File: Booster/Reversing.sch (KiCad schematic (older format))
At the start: 22 parts

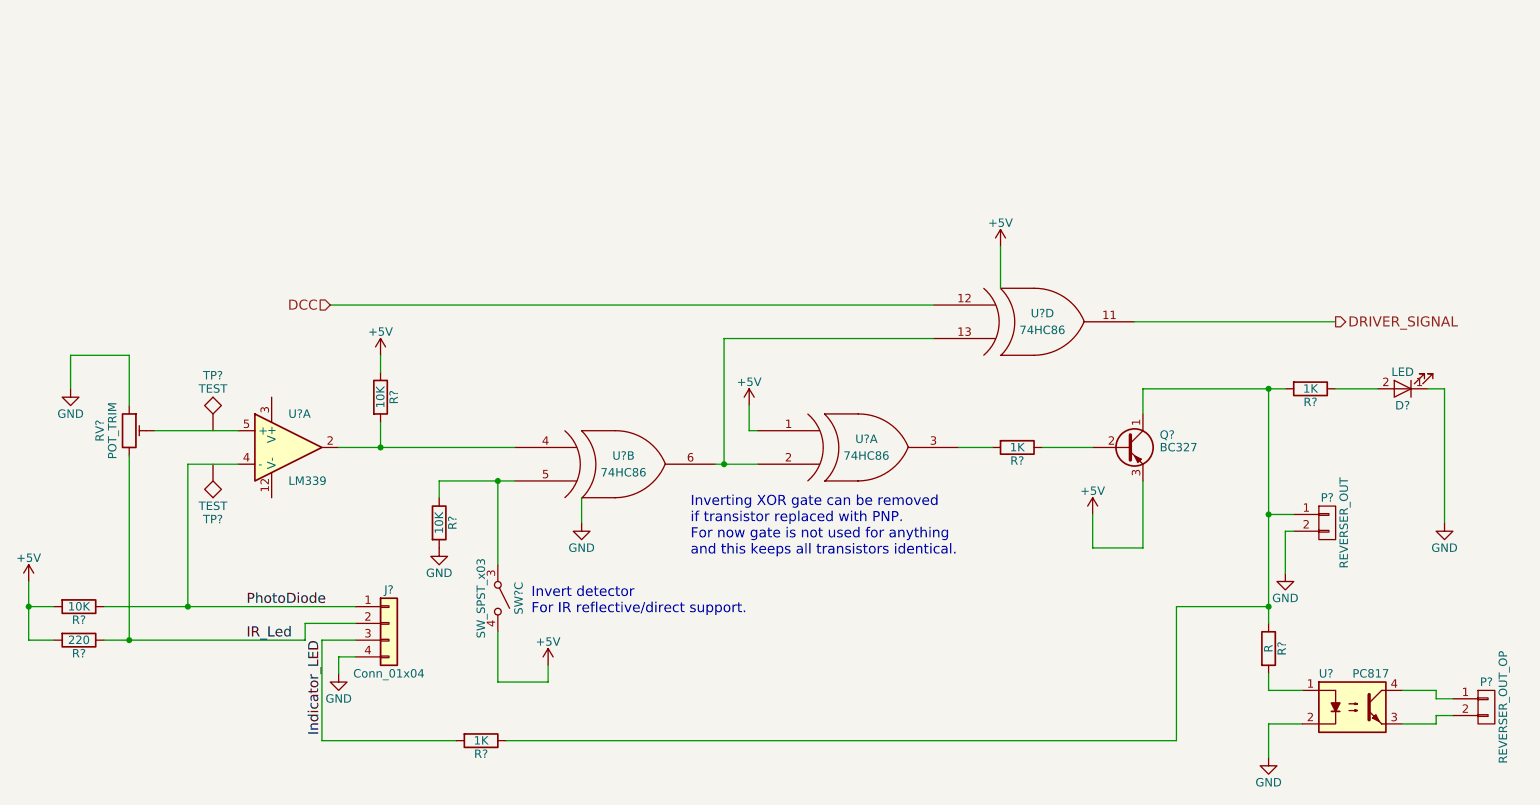
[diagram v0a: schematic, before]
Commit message: Fixed missing connections.
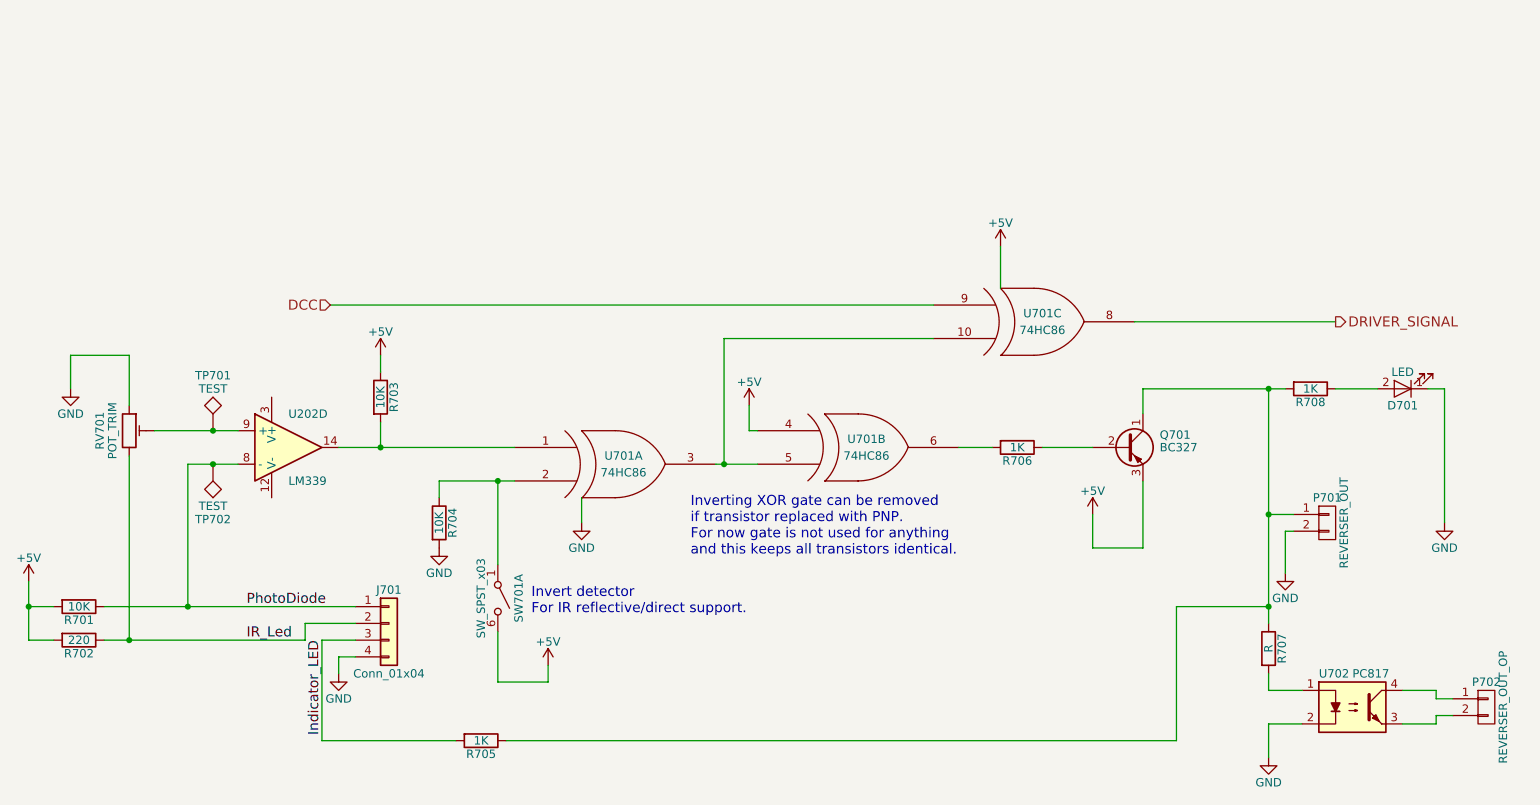
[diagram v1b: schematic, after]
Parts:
- gave numbers to parts that had none: 20
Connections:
- net +5V: now also SW701.6 (B), U701.4 (IN1); no longer SW701.4 (B), U701.1 (IN1)
- net DCC: now also U701.9 (IN1); no longer U701.12 (IN1)
- net DRIVER_SIGNAL: now also U701.8 (OUT); no longer U701.11 (OUT)
- net PhotoDiode: now also TP702.1, U202.8 (-); no longer U202.4 (-)
- net at RV701.2: now also TP701.1, U202.9 (+); no longer U202.5 (+)
- net at R706.2: now also U701.6 (OUT); no longer U701.3 (OUT)
- new net: U701.10 (IN2), U701.3 (OUT), U701.5 (IN2)
- new net: R703.2, U202.14, U701.1 (IN1)
- new net: R704.1, SW701.1 (A), U701.2 (IN2)

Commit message: Pulse detector circuit included.
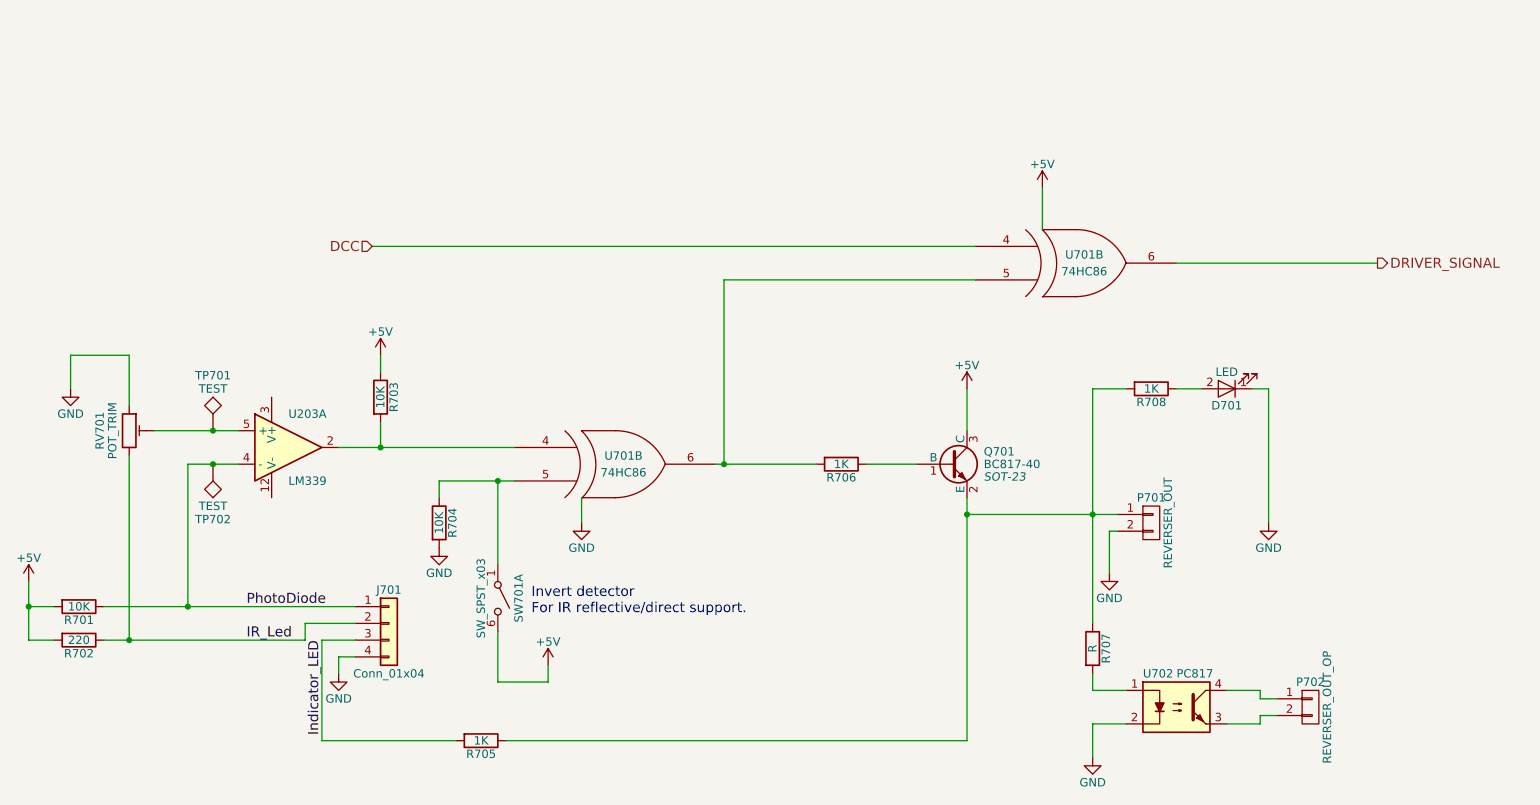
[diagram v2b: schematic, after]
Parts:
- removed Q701: BC327, TO_SOT_Packages_THT:TO-92_Molded_Narrow, symbol BC327
- removed unit 2 of U701
- added Q701: BC817-40, SOT-23, symbol BC817-40
- renumbered U202 to U203
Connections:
- net +5V: now also Q701.3 (C)
- net DCC: now also U701.4 (IN1); no longer U701.9 (IN1)
- net DRIVER_SIGNAL: now also U701.6 (OUT); no longer U701.8 (OUT)
- net PhotoDiode: now also U203.4 (-); no longer U203.8 (-)
- net at RV701.2, TP701.1: now also U203.5 (+); no longer U203.9 (+)
- net at R706.1: now also Q701.1 (B)
- net at R706.2: now also U701.5 (IN2), U701.6 (OUT)
- net at P701.1 (P1), R705.1, R707.1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: now also Q701.2 (E)
- net at R704.1, SW701.1 (A): now also U701.5 (IN2); no longer U701.2 (IN2)
- new net: R703.2, U203.2, U701.4 (IN1)
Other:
- note removed: "Inverting XOR gate can be removed\nif transistor replaced with PNP.\nFor now gate is not used for anything\nand this keeps all transistors identical."
- moved on the sheet: D701, P701, P702, R706, R707, R708, U702

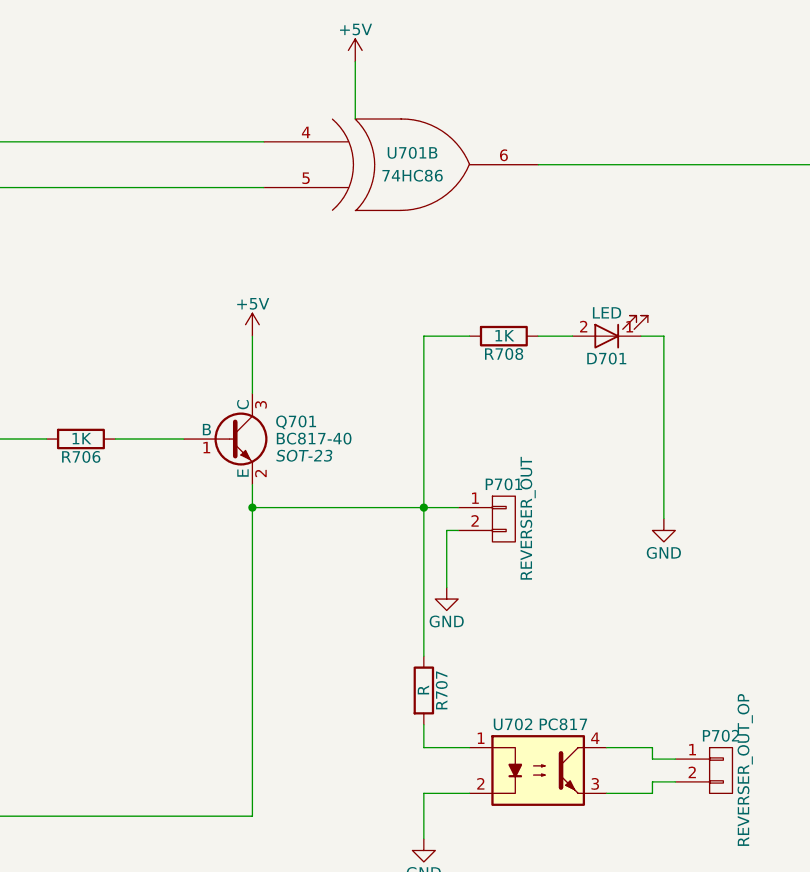
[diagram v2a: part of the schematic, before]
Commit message: Various adjustments based on breadboard prototype.
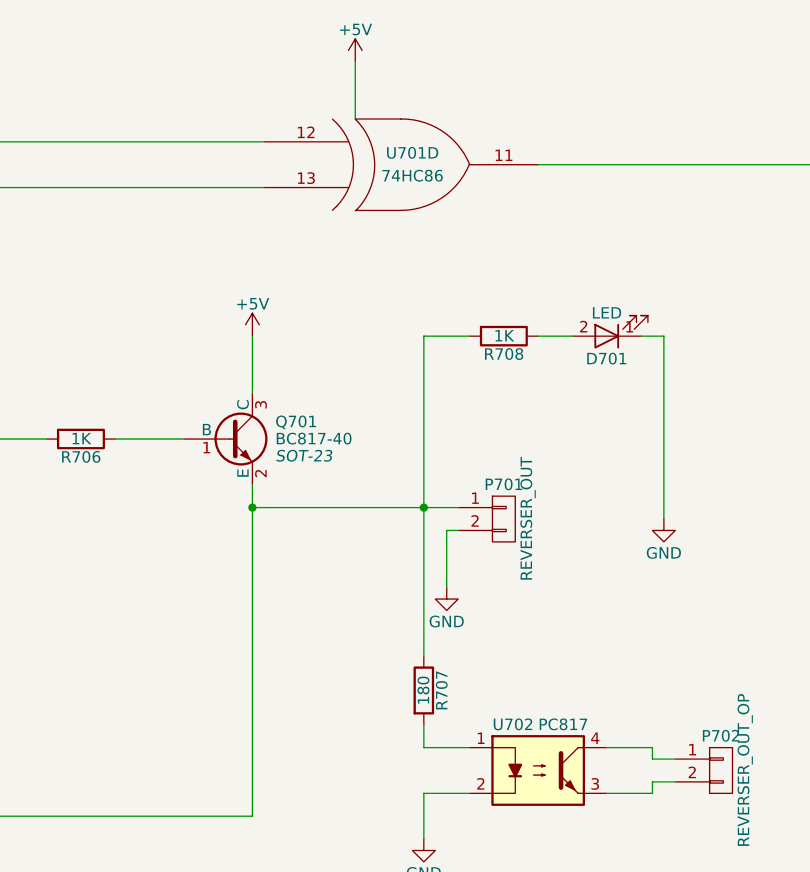
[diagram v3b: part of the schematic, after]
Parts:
- R707: value R -> 180
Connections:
- net DCC: now also U701.12 (IN1); no longer U701.4 (IN1)
- net DRIVER_SIGNAL: now also U701.11 (OUT); no longer U701.6 (OUT)
- net at R706.2, U701.6 (OUT): now also U701.13 (IN2); no longer U701.5 (IN2)
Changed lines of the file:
@@
 $Comp
 L 74LS86 U701
-U 2 1 5A0898F2
+U 4 1 5A0898F2
 P 8200 2250
 F 0 "U701" H 8250 2300 50  0000 C CNN
@@
 F 2 "" H 8200 2250 50  0000 C CNN
 F 3 "" H 8200 2250 50  0000 C CNN
-	2    8200 2250
+	4    8200 2250
 	1    0    0    -1
 $EndComp
@@
 $EndComp
 $Comp
-L +5V #PWR704
+L +5V #PWR053
 U 1 1 5A08A3B3
 P 4050 2800
-F 0 "#PWR704" H 4050 2650 50  0001 C CNN
+F 0 "#PWR053" H 4050 2650 50  0001 C CNN
 F 1 "+5V" H 4050 2940 50  0000 C CNN
 F 2 "" H 4050 2800 50  0000 C CNN
@@
 $EndComp
 $Comp
-L +5V #PWR708
+L +5V #PWR054
 U 1 1 5A08AC26
 P 7550 3000
-F 0 "#PWR708" H 7550 2850 50  0001 C CNN
+F 0 "#PWR054" H 7550 2850 50  0001 C CNN
 F 1 "+5V" H 7550 3140 50  0000 C CNN
 F 2 "" H 7550 3000 50  0000 C CNN
@@
 $EndComp
 $Comp
-L GND #PWR712
+L GND #PWR055
 U 1 1 5A08AC50
 P 9350 3800
-F 0 "#PWR712" H 9350 3550 50  0001 C CNN
+F 0 "#PWR055" H 9350 3550 50  0001 C CNN
 F 1 "GND" H 9350 3650 50  0000 C CNN
 F 2 "" H 9350 3800 50  0000 C CNN
@@
 $EndComp
 $Comp
-L GND #PWR711
+L GND #PWR056
 U 1 1 5A0EF583
 P 8400 4100
-F 0 "#PWR711" H 8400 3850 50  0001 C CNN
+F 0 "#PWR056" H 8400 3850 50  0001 C CNN
 F 1 "GND" H 8400 3950 50  0000 C CNN
 F 2 "" H 8400 4100 50  0001 C CNN
@@
 P 8300 4550
 F 0 "R707" V 8380 4550 50  0000 C CNN
-F 1 "R" V 8300 4550 50  0000 C CNN
+F 1 "180" V 8300 4550 50  0000 C CNN
 F 2 "" V 8230 4550 50  0001 C CNN
 F 3 "" H 8300 4550 50  0001 C CNN
@@
 $EndComp
 $Comp
-L GND #PWR710
+L GND #PWR057
 U 1 1 5A0EF7FA
 P 8300 5200
-F 0 "#PWR710" H 8300 4950 50  0001 C CNN
+F 0 "#PWR057" H 8300 4950 50  0001 C CNN
 F 1 "GND" H 8300 5050 50  0000 C CNN
 F 2 "" H 8300 5200 50  0001 C CNN
@@
 $EndComp
 $Comp
-L GND #PWR705
+L GND #PWR058
 U 1 1 5A0F5794
 P 4400 3950
-F 0 "#PWR705" H 4400 3700 50  0001 C CNN
+F 0 "#PWR058" H 4400 3700 50  0001 C CNN
 F 1 "GND" H 4400 3800 50  0000 C CNN
 F 2 "" H 4400 3950 50  0000 C CNN
@@
 $EndComp
 $Comp
-L +5V #PWR706
+L +5V #PWR059
 U 1 1 5A0F5A28
 P 5050 4650
-F 0 "#PWR706" H 5050 4500 50  0001 C CNN
+F 0 "#PWR059" H 5050 4500 50  0001 C CNN
 F 1 "+5V" H 5050 4790 50  0000 C CNN
 F 2 "" H 5050 4650 50  0001 C CNN
@@
 IR_Led
 $Comp
-L +5V #PWR709
+L +5V #PWR060
 U 1 1 5A0FEE2F
 P 8000 1800
-F 0 "#PWR709" H 8000 1650 50  0001 C CNN
+F 0 "#PWR060" H 8000 1650 50  0001 C CNN
 F 1 "+5V" H 8000 1940 50  0000 C CNN
 F 2 "" H 8000 1800 50  0001 C CNN
@@
 	3800 4600 3800 4700
 $Comp
-L GND #PWR703
+L GND #PWR061
 U 1 1 5A101A8A
 P 3800 4700
-F 0 "#PWR703" H 3800 4450 50  0001 C CNN
+F 0 "#PWR061" H 3800 4450 50  0001 C CNN
 F 1 "GND" H 3800 4550 50  0000 C CNN
 F 2 "" H 3800 4700 50  0001 C CNN
@@
 $EndComp
 $Comp
-L +5V #PWR701
+L +5V #PWR062
 U 1 1 5A104760
 P 1950 4150
-F 0 "#PWR701" H 1950 4000 50  0001 C CNN
+F 0 "#PWR062" H 1950 4000 50  0001 C CNN
 F 1 "+5V" H 1950 4290 50  0000 C CNN
 F 2 "" H 1950 4150 50  0001 C CNN
@@
 	2200 2800 2200 3000
 $Comp
-L GND #PWR702
+L GND #PWR063
 U 1 1 5A19FF1E
 P 2200 3000
-F 0 "#PWR702" H 2200 2750 50  0001 C CNN
+F 0 "#PWR063" H 2200 2750 50  0001 C CNN
 F 1 "GND" H 2200 2850 50  0000 C CNN
 F 2 "" H 2200 3000 50  0000 C CNN
@@
 $EndComp
 $Comp
-L GND #PWR707
+L GND #PWR064
 U 1 1 5A397E1F
 P 5250 3800
-F 0 "#PWR707" H 5250 3550 50  0001 C CNN
+F 0 "#PWR064" H 5250 3550 50  0001 C CNN
 F 1 "GND" H 5250 3650 50  0000 C CNN
 F 2 "" H 5250 3800 50  0001 C CNN
